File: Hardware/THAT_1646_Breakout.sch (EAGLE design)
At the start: 30 parts, among them IC1 THAT1646, J1 1x4, J2 SN, J3 S, J4 TN, J5 RN, J6 OUTPUT, J7 T, J8 R, J9 Chassis

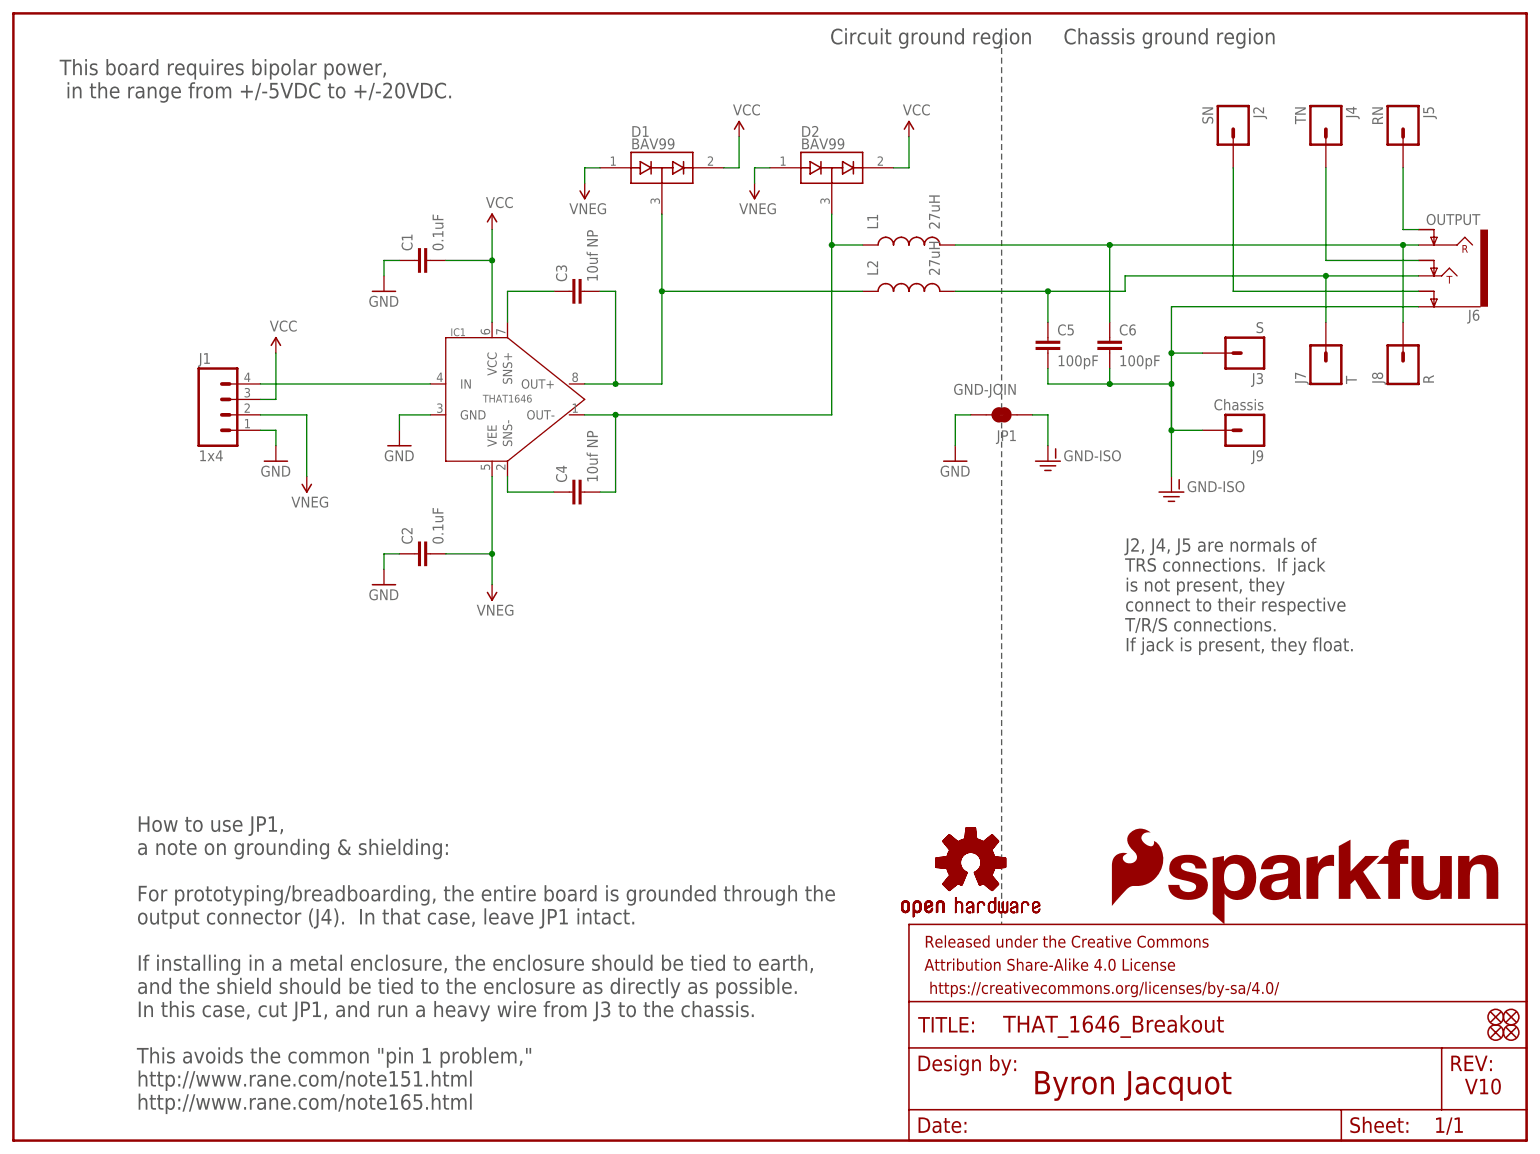
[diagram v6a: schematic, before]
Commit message: Updates from engineering checklist.
Found too-narrow silk in some packages.
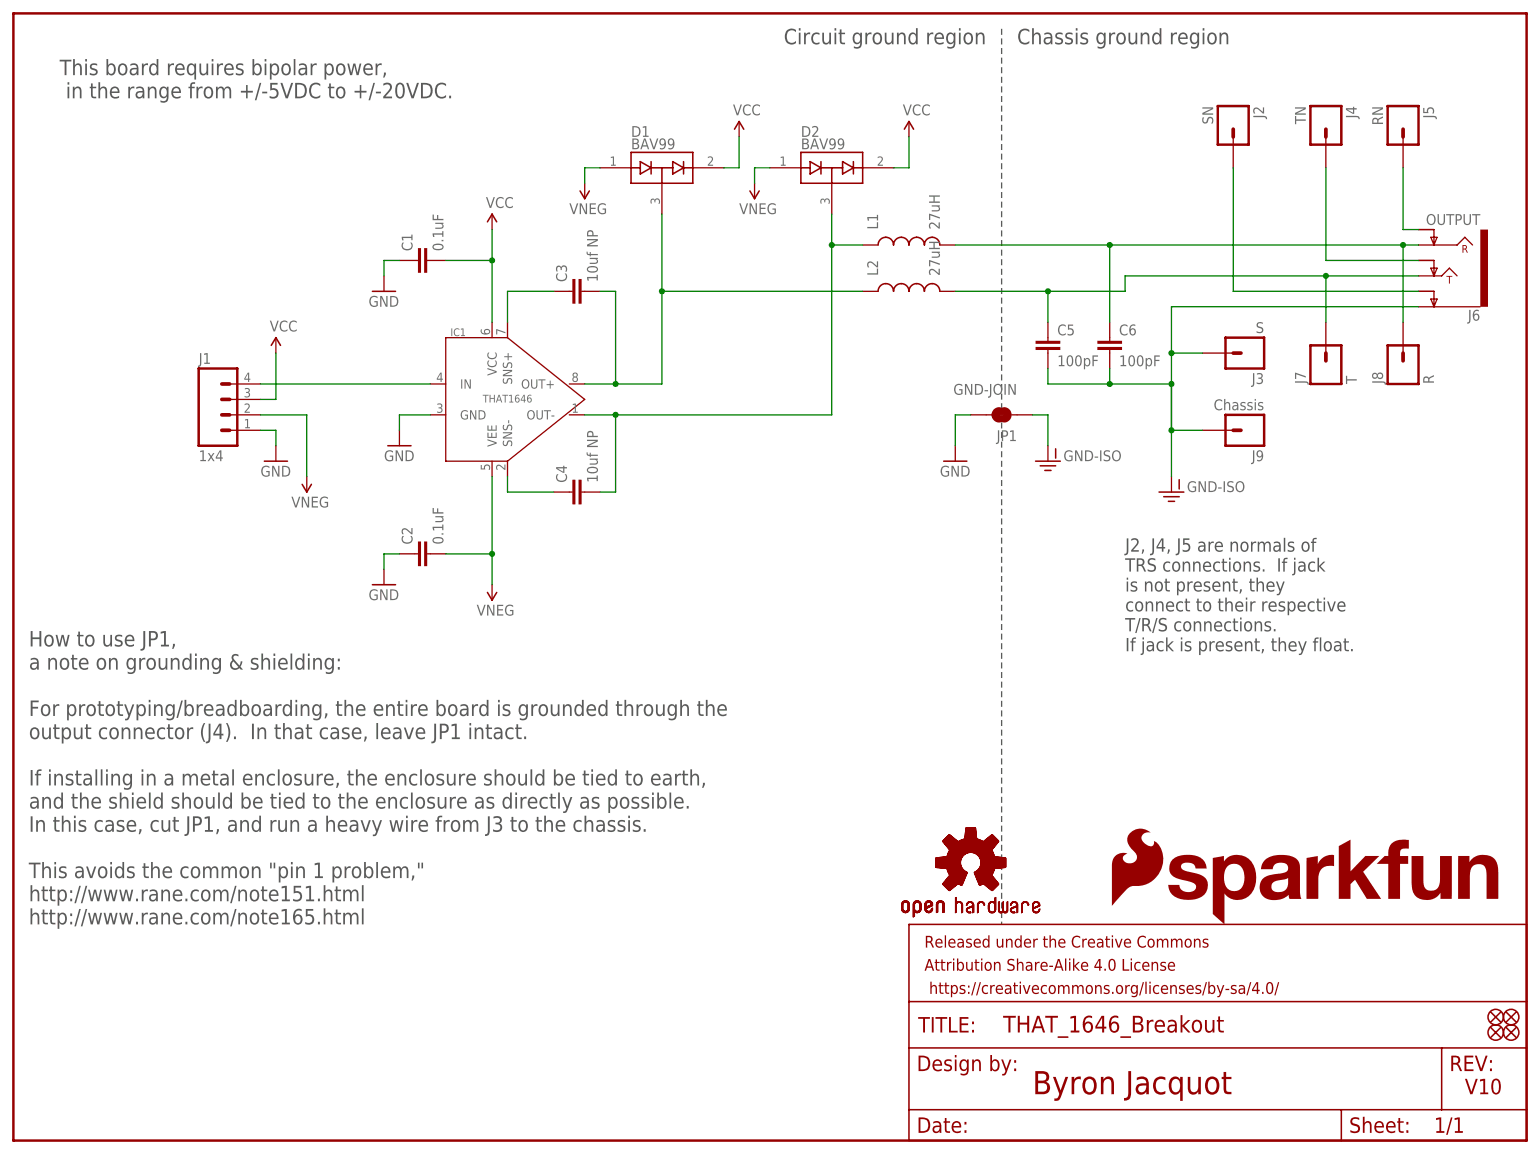
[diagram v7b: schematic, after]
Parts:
- J6: device SparkFun-Connectors:AUDIO-JACK4-.25-HORIZ-TRS -> SparkFun-Connectors:AUDIO_JACK_TRS_0.25"_PTH_RA
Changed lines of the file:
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@@
 <parts>
 <part name="FRAME1" library="SparkFun-Aesthetics" deviceset="FRAME-LETTER" device=""/>
-<part name="J6" library="SparkFun-Connectors" deviceset="AUDIO-JACK4-.25-HORIZ-TRS" device="" value="OUTPUT"/>
+<part name="J6" library="SparkFun-Connectors" deviceset="AUDIO_JACK_TRS_0.25&quot;_PTH_RA" device="" value="OUTPUT"/>
 <part name="SUPPLY3" library="SparkFun-Aesthetics" deviceset="VCC" device=""/>
 <part name="GND-ISO2" library="SparkFun-Aesthetics" deviceset="GND-ISO" device=""/>
@@
 <text x="238.76" y="7.62" size="2.54" layer="94" font="vector">V10</text>
 <wire x1="162.56" y1="182.88" x2="162.56" y2="35.56" width="0.2032" layer="97" style="longdash"/>
-<text x="172.72" y="180.34" size="2.54" layer="97" font="vector" rot="R180" align="top-right">Chassis ground region</text>
-<text x="167.64" y="180.34" size="2.54" layer="97" font="vector" rot="R180" align="top-left">Circuit ground region</text>
-<text x="20.32" y="53.34" size="2.54" layer="97" align="top-left">How to use JP1,
+<text x="165.1" y="180.34" size="2.54" layer="97" font="vector" rot="R180" align="top-right">Chassis ground region</text>
+<text x="160.02" y="180.34" size="2.54" layer="97" font="vector" rot="R180" align="top-left">Circuit ground region</text>
+<text x="2.54" y="83.82" size="2.54" layer="97" align="top-left">How to use JP1,
 a note on grounding &amp; shielding:
 For prototyping/breadboarding, the entire board is grounded through the
